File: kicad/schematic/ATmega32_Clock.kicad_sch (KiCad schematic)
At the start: 20 parts, among them J1 USART, J2 ISP, SW1 RESET, SW2 SET, SW3 INCREMENT, SW4 CLK_RST, U1 ATmega32A-P, Y1 8MHz

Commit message: Add complete wiring and net labels connecting MCU pins to all peripherals
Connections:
- net CLOCK_RESET: now also R4.2, SW4.2
- net GND: now also J2.6 (Pin_6)
- net INC_BTN: now also R3.2, SW3.2
- net LED_STATUS: now also R5.1, R6.1
- net MISO: now also J2.4 (Pin_4)
- net MOSI: now also J2.5 (Pin_5)
- net SCK: now also J2.3 (Pin_3)
- net SET_BTN: now also R2.2, SW2.2
- net VCC: now also C4.1, J2.2 (Pin_2)
- net at Y1.1: now also Y1.2
- net ~{RESET}: now reaches R1.2, SW1.2
- net ~{RESET}: now also J2.1 (Pin_1)
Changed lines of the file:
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@@
     (at 182.88 63.5 0) (effects (font (size 1.27 1.27)))
   )
+  (wire (pts (xy 137.16 63.5) (xy 107.95 63.5)) (stroke (width 0) (type default)))
+  (wire (pts (xy 107.95 63.5) (xy 107.95 82.55)) (stroke (width 0) (type default)))
+  (wire (pts (xy 115.57 74.93) (xy 115.57 63.5)) (stroke (width 0) (type default)))
+  (wire (pts (xy 137.16 68.58) (xy 123.19 68.58)) (stroke (width 0) (type default)))
+  (wire (pts (xy 123.19 68.58) (xy 123.19 82.55)) (stroke (width 0) (type default)))
+  (wire (pts (xy 115.57 82.55) (xy 115.57 68.58)) (stroke (width 0) (type default)))
+  (wire (pts (xy 137.16 58.42) (xy 121.92 58.42)) (stroke (width 0) (type default)))
+  (wire (pts (xy 121.92 58.42) (xy 121.92 59.69)) (stroke (width 0) (type default)))
+  (wire (pts (xy 154.94 50.8) (xy 154.94 44.45)) (stroke (width 0) (type default)))
+  (wire (pts (xy 154.94 44.45) (xy 157.48 44.45)) (stroke (width 0) (type default)))
+  (wire (pts (xy 157.48 44.45) (xy 157.48 40)) (stroke (width 0) (type default)))
+  (wire (pts (xy 157.48 52.07) (xy 157.48 55)) (stroke (width 0) (type default)))
+  (wire (pts (xy 165.1 44.45) (xy 165.1 40)) (stroke (width 0) (type default)))
+  (wire (pts (xy 165.1 52.07) (xy 165.1 55)) (stroke (width 0) (type default)))
+  (wire (pts (xy 152.4 38.1) (xy 165.1 38.1)) (stroke (width 0) (type default)))
+  (wire (pts (xy 157.48 38.1) (xy 157.48 40)) (stroke (width 0) (type default)))
+  (wire (pts (xy 165.1 38.1) (xy 165.1 40)) (stroke (width 0) (type default)))
+  (wire (pts (xy 157.48 55) (xy 157.48 57)) (stroke (width 0) (type default)))
+  (wire (pts (xy 165.1 55) (xy 165.1 57)) (stroke (width 0) (type default)))
+  (wire (pts (xy 113.03 114.3) (xy 119.38 114.3)) (stroke (width 0) (type default)))
+  (wire (pts (xy 113.03 111.76) (xy 119.38 111.76)) (stroke (width 0) (type default)))
+  (wire (pts (xy 167.64 127.0) (xy 177.8 127.0)) (stroke (width 0) (type default)))
+  (label "USART_RXD" (at 177.8 127.0 0) (effects (font (size 1.27 1.27))))
+  (wire (pts (xy 167.64 129.54) (xy 177.8 129.54)) (stroke (width 0) (type default)))
+  (label "USART_TXD" (at 177.8 129.54 0) (effects (font (size 1.27 1.27))))
+  (wire (pts (xy 83.82 85.09) (xy 81.28 85.09)) (stroke (width 0) (type default)))
+  (wire (pts (xy 83.82 82.55) (xy 81.28 82.55)) (stroke (width 0) (type default)))
+  (wire (pts (xy 97.79 82.55) (xy 96.52 82.55)) (stroke (width 0) (type default)))
+  (wire (pts (xy 167.64 93.98) (xy 177.8 93.98)) (stroke (width 0) (type default)))
+  (label "MOSI" (at 177.8 93.98 0) (effects (font (size 1.27 1.27))))
+  (wire (pts (xy 167.64 96.52) (xy 177.8 96.52)) (stroke (width 0) (type default)))
+  (label "MISO" (at 177.8 96.52 0) (effects (font (size 1.27 1.27))))
+  (wire (pts (xy 167.64 99.06) (xy 177.8 99.06)) (stroke (width 0) (type default)))
+  (label "SCK" (at 177.8 99.06 0) (effects (font (size 1.27 1.27))))
+  (wire (pts (xy 83.82 80.01) (xy 80 80.01)) (stroke (width 0) (type default)))
+  (label "~{RESET}" (at 80 80.01 180) (effects (font (size 1.27 1.27))))
+  (wire (pts (xy 137.16 58.42) (xy 135 58.42)) (stroke (width 0) (type default)))
+  (label "~{RESET}" (at 135 58.42 180) (effects (font (size 1.27 1.27))))
+  (wire (pts (xy 96.52 80.01) (xy 98 80.01)) (stroke (width 0) (type default)))
+  (label "VCC" (at 98 80.01 0) (effects (font (size 1.27 1.27))))
+  (wire (pts (xy 96.52 85.09) (xy 98 85.09)) (stroke (width 0) (type default)))
+  (label "GND" (at 98 85.09 0) (effects (font (size 1.27 1.27))))
+  (wire (pts (xy 167.64 81.28) (xy 177.8 81.28)) (stroke (width 0) (type default)))
+  (label "LED_STATUS" (at 177.8 81.28 0) (effects (font (size 1.27 1.27))))
+  (wire (pts (xy 195.58 72.39) (xy 195.58 70)) (stroke (width 0) (type default)))
+  (label "LED_STATUS" (at 195.58 70 90) (effects (font (size 1.27 1.27))))
+  (wire (pts (xy 167.64 83.82) (xy 177.8 83.82)) (stroke (width 0) (type default)))
+  (label "LED_TASK" (at 177.8 83.82 0) (effects (font (size 1.27 1.27))))
+  (wire (pts (xy 208.28 72.39) (xy 208.28 70)) (stroke (width 0) (type default)))
+  (label "LED_TASK" (at 208.28 70 90) (effects (font (size 1.27 1.27))))
+  (wire (pts (xy 167.64 58.42) (xy 177.8 58.42)) (stroke (width 0) (type default)))
+  (label "SET_BTN" (at 177.8 58.42 0) (effects (font (size 1.27 1.27))))
+  (wire (pts (xy 167.64 60.96) (xy 177.8 60.96)) (stroke (width 0) (type default)))
+  (label "INC_BTN" (at 177.8 60.96 0) (effects (font (size 1.27 1.27))))
+  (wire (pts (xy 167.64 63.5) (xy 177.8 63.5)) (stroke (width 0) (type default)))
+  (label "CLOCK_RESET" (at 177.8 63.5 0) (effects (font (size 1.27 1.27))))
+  (wire (pts (xy 195.58 125.73) (xy 192 125.73)) (stroke (width 0) (type default)))
+  (label "SET_BTN" (at 192 125.73 180) (effects (font (size 1.27 1.27))))
+  (wire (pts (xy 208.28 125.73) (xy 205 125.73)) (stroke (width 0) (type default)))
+  (label "INC_BTN" (at 205 125.73 180) (effects (font (size 1.27 1.27))))
+  (wire (pts (xy 220.98 125.73) (xy 217 125.73)) (stroke (width 0) (type default)))
+  (label "CLOCK_RESET" (at 217 125.73 180) (effects (font (size 1.27 1.27))))
   (sheet_instances
     (path "/" (page "1"))

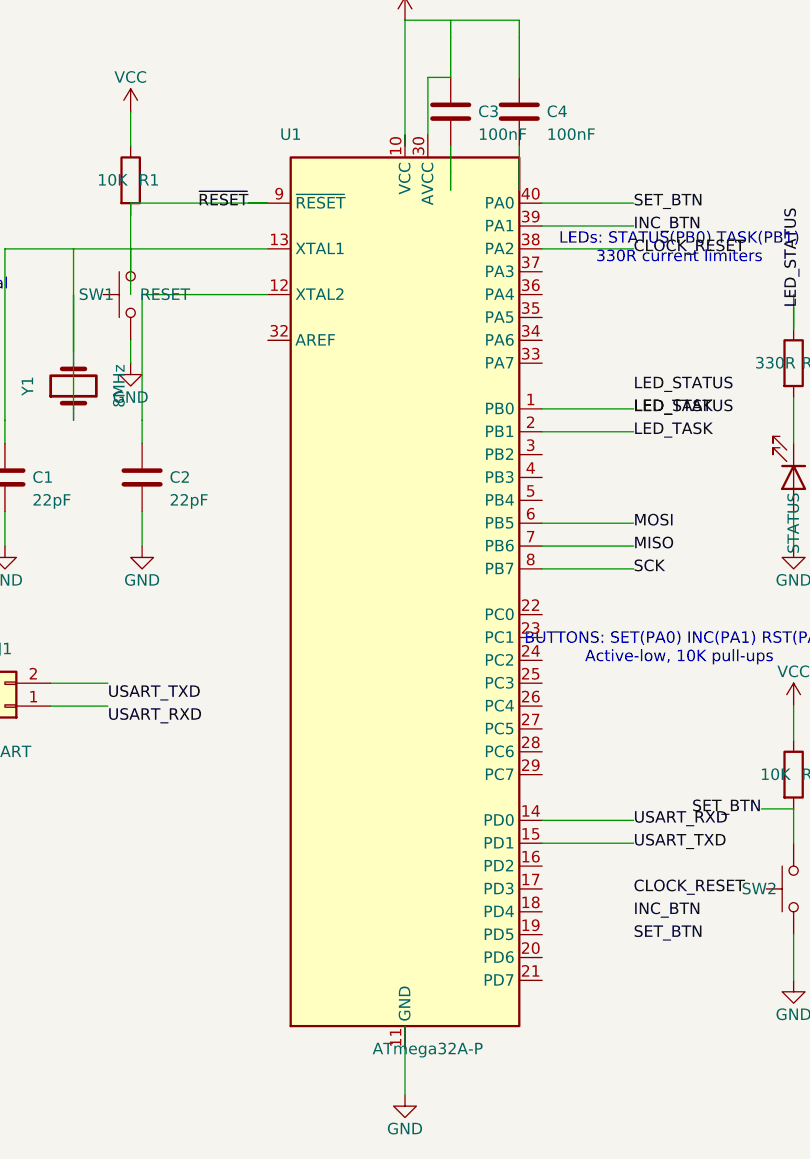
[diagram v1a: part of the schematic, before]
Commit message: Fix MCU symbol: replace extends with self-contained ATmega32A-P definition - chip now renders correctly
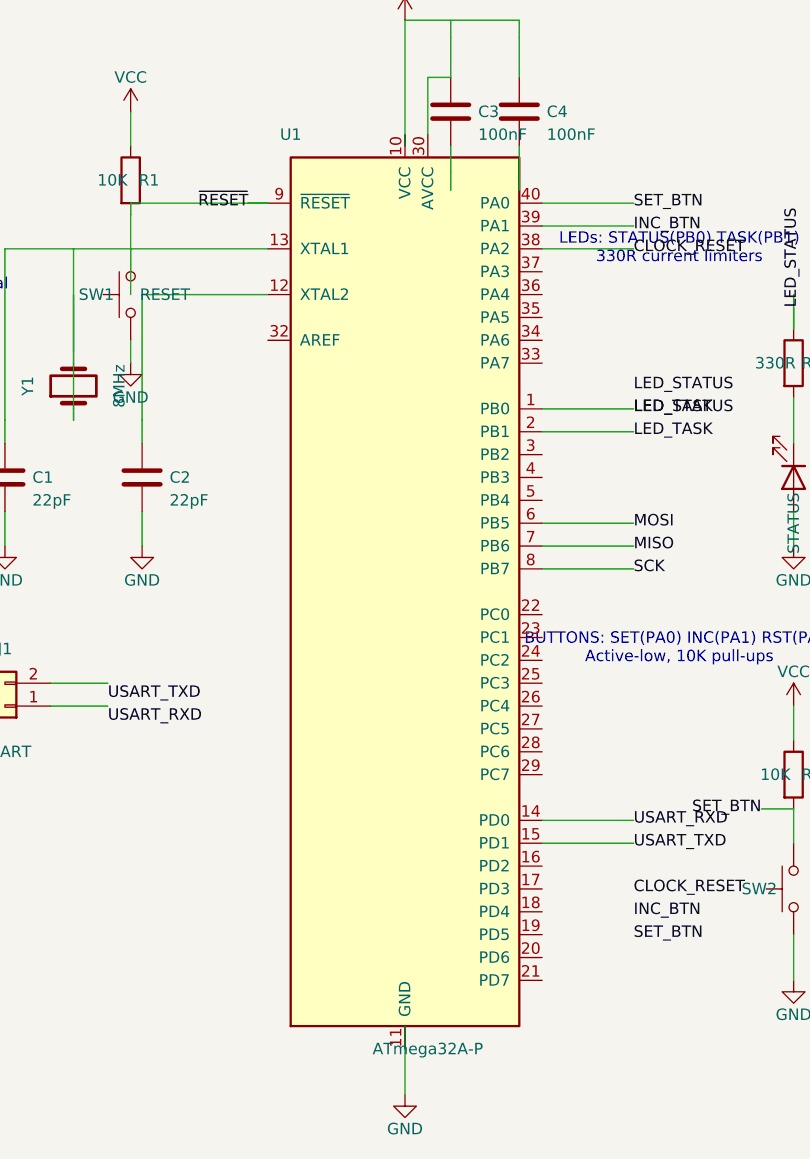
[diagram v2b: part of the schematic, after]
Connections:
- net CLOCK_RESET: now also U1.38 (PA2)
- net INC_BTN: now also U1.39 (PA1)
- net LED_STATUS: now also U1.1 (PB0), U1.2 (PB1)
- net MISO: now also U1.7 (PB6)
- net MOSI: now also U1.6 (PB5)
- net SCK: now also U1.8 (PB7)
- net SET_BTN: now also U1.40 (PA0)
- net USART_RXD: now also U1.14 (PD0)
- net USART_TXD: now also U1.15 (PD1)
- net ~{RESET}: now also U1.9 (~{RESET})
- net at C1.1: now also U1.13 (XTAL1)
- net at C2.1: now also U1.12 (XTAL2)
- net at C3.1: now also U1.30 (AVCC)
- new net: U1.11 (GND), U1.31 (GND)

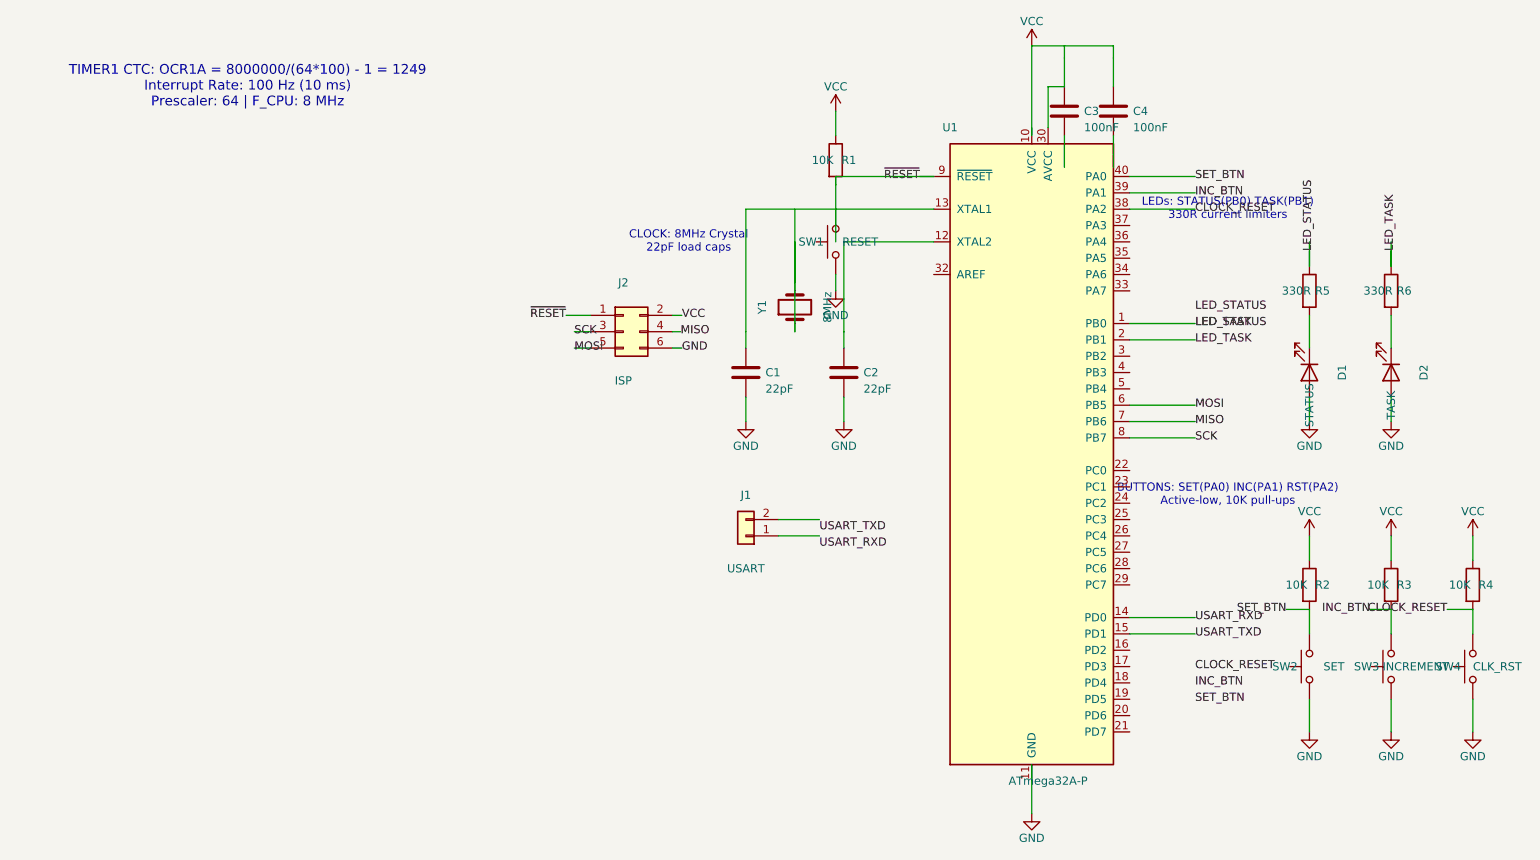
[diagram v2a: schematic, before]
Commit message: Complete schematic wiring: all MCU pins correctly connected to peripherals via net labels
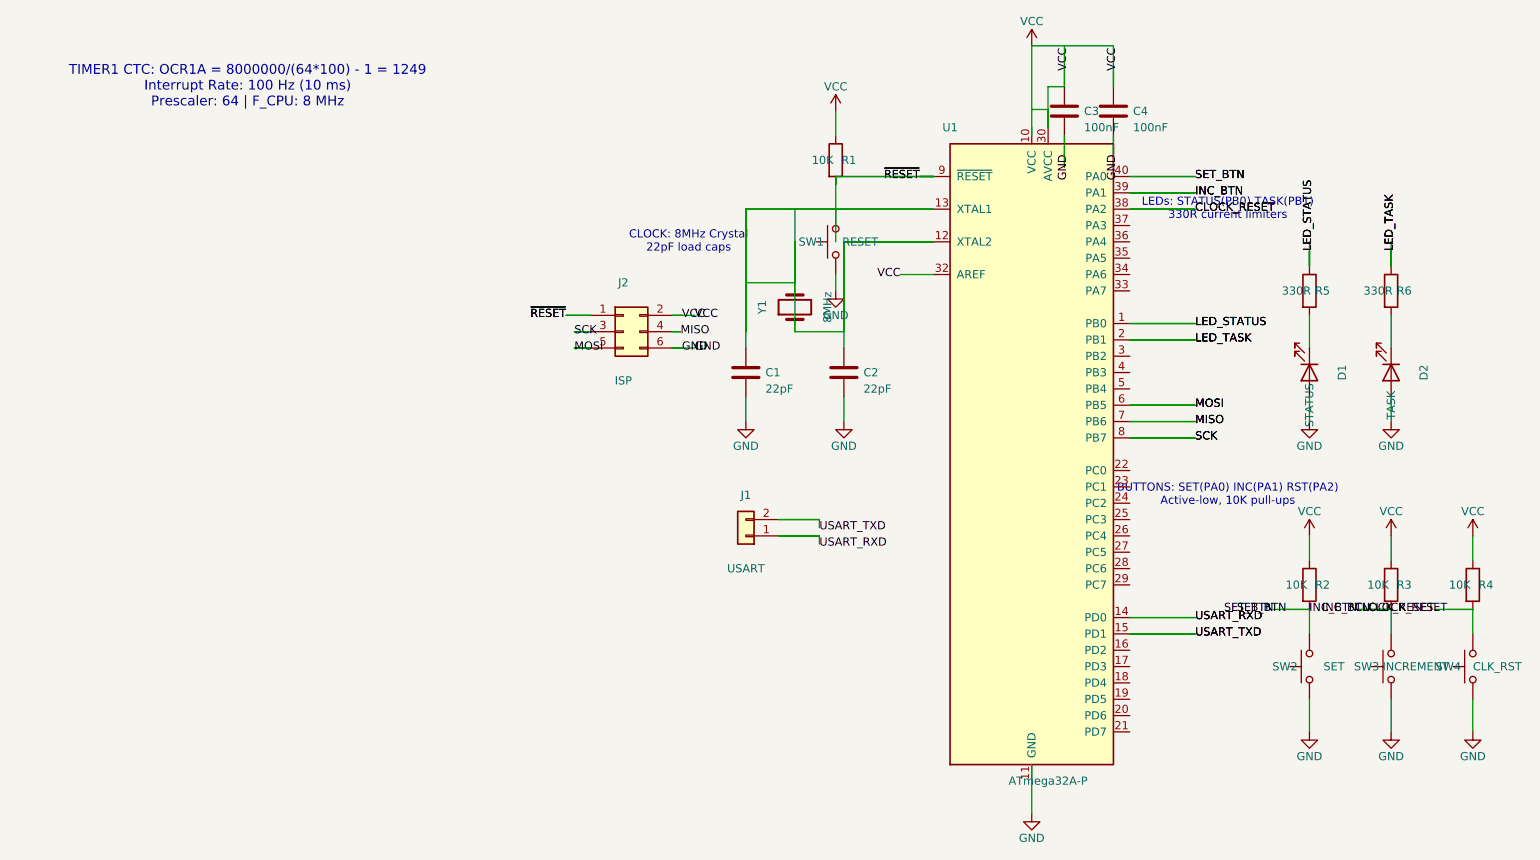
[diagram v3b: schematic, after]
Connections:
- net GND: now also C3.2, C4.2
- net LED_STATUS: no longer R6.1, U1.2 (PB1)
- net USART_RXD: now also J1.1 (Pin_1)
- net USART_TXD: now also J1.2 (Pin_2)
- net VCC: now also C3.1, U1.30 (AVCC), U1.32 (AREF)
- net at C2.1, U1.12 (XTAL2): now also C1.1, U1.13 (XTAL1), Y1.1, Y1.2
- new net LED_TASK: R6.1, U1.2 (PB1)
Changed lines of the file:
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@@
     (instances (project "ATmega32_Clock" (path "/e63e39d7-6ac0-4ffd-8aa3-1841a4541b55" (reference "#PWR014") (unit 1))))
   )
-  (label "SET_BTN" (at 177.8 139.7 0) (effects (font (size 1.27 1.27))))
-  (label "INC_BTN" (at 177.8 137.16 0) (effects (font (size 1.27 1.27))))
-  (label "CLOCK_RESET" (at 177.8 134.62 0) (effects (font (size 1.27 1.27))))
-  (label "LED_STATUS" (at 177.8 78.74 0) (effects (font (size 1.27 1.27))))
-  (label "LED_TASK" (at 177.8 81.28 0) (effects (font (size 1.27 1.27))))
+  (label "SET_BTN" (at 177.8 58.42 0) (effects (font (size 1.27 1.27))))
+  (label "INC_BTN" (at 177.8 60.96 0) (effects (font (size 1.27 1.27))))
+  (label "CLOCK_RESET" (at 177.8 63.5 0) (effects (font (size 1.27 1.27))))
+  (label "LED_STATUS" (at 177.8 81.28 0) (effects (font (size 1.27 1.27))))
+  (label "LED_TASK" (at 177.8 83.82 0) (effects (font (size 1.27 1.27))))
   (label "USART_TXD" (at 119.38 113.03 0) (effects (font (size 1.27 1.27))))
   (label "USART_RXD" (at 119.38 115.57 0) (effects (font (size 1.27 1.27))))
@@
   (wire (pts (xy 220.98 125.73) (xy 217 125.73)) (stroke (width 0) (type default)))
   (label "CLOCK_RESET" (at 217 125.73 180) (effects (font (size 1.27 1.27))))
+  (wire (pts (xy 167.64 81.28) (xy 177.8 81.28)) (stroke (width 0) (type default)))
+  (wire (pts (xy 167.64 83.82) (xy 177.8 83.82)) (stroke (width 0) (type default)))
+  (wire (pts (xy 167.64 58.42) (xy 177.8 58.42)) (stroke (width 0) (type default)))
+  (wire (pts (xy 167.64 60.96) (xy 177.8 60.96)) (stroke (width 0) (type default)))
+  (wire (pts (xy 167.64 63.5) (xy 177.8 63.5)) (stroke (width 0) (type default)))
+  (wire (pts (xy 167.64 127.0) (xy 177.8 127.0)) (stroke (width 0) (type default)))
+  (label "USART_RXD" (at 177.8 127.0 0) (effects (font (size 1.27 1.27))))
+  (wire (pts (xy 167.64 129.54) (xy 177.8 129.54)) (stroke (width 0) (type default)))
+  (label "USART_TXD" (at 177.8 129.54 0) (effects (font (size 1.27 1.27))))
+  (wire (pts (xy 167.64 93.98) (xy 177.8 93.98)) (stroke (width 0) (type default)))
+  (label "MOSI" (at 177.8 93.98 0) (effects (font (size 1.27 1.27))))
+  (wire (pts (xy 167.64 96.52) (xy 177.8 96.52)) (stroke (width 0) (type default)))
+  (label "MISO" (at 177.8 96.52 0) (effects (font (size 1.27 1.27))))
+  (wire (pts (xy 167.64 99.06) (xy 177.8 99.06)) (stroke (width 0) (type default)))
+  (label "SCK" (at 177.8 99.06 0) (effects (font (size 1.27 1.27))))
+  (wire (pts (xy 137.16 58.42) (xy 121.92 58.42)) (stroke (width 0) (type default)))
+  (wire (pts (xy 121.92 58.42) (xy 121.92 59.69)) (stroke (width 0) (type default)))
+  (wire (pts (xy 137.16 63.5) (xy 107.95 63.5)) (stroke (width 0) (type default)))
+  (wire (pts (xy 107.95 63.5) (xy 107.95 74.93)) (stroke (width 0) (type default)))
+  (wire (pts (xy 115.57 74.93) (xy 107.95 74.93)) (stroke (width 0) (type default)))
+  (wire (pts (xy 107.95 74.93) (xy 107.95 82.55)) (stroke (width 0) (type default)))
+  (wire (pts (xy 137.16 68.58) (xy 123.19 68.58)) (stroke (width 0) (type default)))
+  (wire (pts (xy 123.19 68.58) (xy 123.19 82.55)) (stroke (width 0) (type default)))
+  (wire (pts (xy 115.57 82.55) (xy 123.19 82.55)) (stroke (width 0) (type default)))
+  (wire (pts (xy 137.16 73.66) (xy 132 73.66)) (stroke (width 0) (type default)))
+  (label "VCC" (at 132 73.66 180) (effects (font (size 1.27 1.27))))
+  (wire (pts (xy 154.94 50.8) (xy 154.94 48)) (stroke (width 0) (type default)))
+  (wire (pts (xy 154.94 48) (xy 152.4 48)) (stroke (width 0) (type default)))
+  (wire (pts (xy 157.48 44.45) (xy 157.48 42)) (stroke (width 0) (type default)))
+  (label "VCC" (at 157.48 42 90) (effects (font (size 1.27 1.27))))
+  (wire (pts (xy 157.48 52.07) (xy 157.48 55)) (stroke (width 0) (type default)))
+  (label "GND" (at 157.48 55 270) (effects (font (size 1.27 1.27))))
+  (wire (pts (xy 165.1 44.45) (xy 165.1 42)) (stroke (width 0) (type default)))
+  (label "VCC" (at 165.1 42 90) (effects (font (size 1.27 1.27))))
+  (wire (pts (xy 165.1 52.07) (xy 165.1 55)) (stroke (width 0) (type default)))
+  (label "GND" (at 165.1 55 270) (effects (font (size 1.27 1.27))))
+  (wire (pts (xy 195.58 72.39) (xy 195.58 70)) (stroke (width 0) (type default)))
+  (label "LED_STATUS" (at 195.58 70 90) (effects (font (size 1.27 1.27))))
+  (wire (pts (xy 208.28 72.39) (xy 208.28 70)) (stroke (width 0) (type default)))
+  (label "LED_TASK" (at 208.28 70 90) (effects (font (size 1.27 1.27))))
+  (wire (pts (xy 195.58 125.73) (xy 190 125.73)) (stroke (width 0) (type default)))
+  (label "SET_BTN" (at 190 125.73 180) (effects (font (size 1.27 1.27))))
+  (wire (pts (xy 208.28 125.73) (xy 203 125.73)) (stroke (width 0) (type default)))
+  (label "INC_BTN" (at 203 125.73 180) (effects (font (size 1.27 1.27))))
+  (wire (pts (xy 220.98 125.73) (xy 215 125.73)) (stroke (width 0) (type default)))
+  (label "CLOCK_RESET" (at 215 125.73 180) (effects (font (size 1.27 1.27))))
+  (wire (pts (xy 113.03 111.76) (xy 119.38 111.76)) (stroke (width 0) (type default)))
+  (wire (pts (xy 119.38 111.76) (xy 119.38 113.03)) (stroke (width 0) (type default)))
+  (wire (pts (xy 113.03 114.3) (xy 119.38 114.3)) (stroke (width 0) (type default)))
+  (wire (pts (xy 119.38 114.3) (xy 119.38 115.57)) (stroke (width 0) (type default)))
+  (wire (pts (xy 83.82 85.09) (xy 81.28 85.09)) (stroke (width 0) (type default)))
+  (wire (pts (xy 83.82 82.55) (xy 81.28 82.55)) (stroke (width 0) (type default)))
+  (wire (pts (xy 96.52 82.55) (xy 97.79 82.55)) (stroke (width 0) (type default)))
+  (wire (pts (xy 96.52 80.01) (xy 100 80.01)) (stroke (width 0) (type default)))
+  (label "VCC" (at 100 80.01 0) (effects (font (size 1.27 1.27))))
+  (wire (pts (xy 96.52 85.09) (xy 100 85.09)) (stroke (width 0) (type default)))
+  (label "GND" (at 100 85.09 0) (effects (font (size 1.27 1.27))))
+  (wire (pts (xy 83.82 80.01) (xy 80 80.01)) (stroke (width 0) (type default)))
+  (label "~{RESET}" (at 80 80.01 180) (effects (font (size 1.27 1.27))))
+  (label "~{RESET}" (at 135 58.42 180) (effects (font (size 1.27 1.27))))
+  (wire (pts (xy 137.16 58.42) (xy 135 58.42)) (stroke (width 0) (type default)))
   (sheet_instances
     (path "/" (page "1"))
